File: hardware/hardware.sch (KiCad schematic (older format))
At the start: 14 parts, among them P1 CONN_13X2, Q1 Q_NPN_BCE, U1 74HC595, U2 74HC595, U3 74HC595, U4 DAC08, U5 DAC08, U6 DAC08, U7 LM555N

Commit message: Finish PWM circuitry
Note that we may have to tune the voltage going to the DAC to taste just
to make sure that Q1 isn't getting too saturated at the base.

Signed-off-by: Nkeck720 <noahkeck72@gmail.com>
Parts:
- removed Q1: Q_NPN_BCE, symbol Q_NPN_BCE
- added Q?: PN2222A, symbol PN2222A
- added U?: NCP1117ST20T3G, TO_SOT_Packages_SMD:SOT-223, symbol NCP1117ST20T3G
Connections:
- wire segments 65 -> 69
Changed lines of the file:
@@
 Wire Wire Line
 	8750 2250 8750 1950
-$Comp
-L Q_NPN_BCE Q1
-U 1 1 592B0265
-P 8850 1400
-F 0 "Q1" H 8750 1600 50  0000 R CNN
-F 1 "Q_NPN_BCE" H 8750 1500 50  0000 R CNN
-F 2 "" H 9050 1500 50  0000 C CNN
-F 3 "" H 8850 1400 50  0000 C CNN
-	1    8850 1400
-	-1   0    0    -1
-$EndComp
 Wire Wire Line
 	8750 1600 8750 1650
@@
 Text Notes 700  5650 0    60   ~ 0
 SCLK/RCLK needs to be set at 300 baud, will a 555 be stable enough or will\nwe need a crystal oscillator?
+$Comp
+L PN2222A Q?
+U 1 1 592B2515
+P 8850 1400
+F 0 "Q?" H 8700 1250 50  0000 L CNN
+F 1 "PN2222A" H 8450 1550 50  0000 L CNN
+F 2 "" H 9050 1325 50  0000 L CIN
+F 3 "" H 8850 1400 50  0000 L CNN
+	1    8850 1400
+	-1   0    0    -1
+$EndComp
+Text GLabel 3100 850  0    60   Input ~ 0
++5
+$Comp
+L NCP1117ST20T3G U?
+U 1 1 592B388B
+P 3600 850
+F 0 "U?" H 3600 1075 50  0000 C CNN
+F 1 "NCP1117ST20T3G" H 3600 1000 50  0000 C CNN
+F 2 "TO_SOT_Packages_SMD:SOT-223" H 3650 600 50  0001 L CNN
+F 3 "" H 3600 850 50  0000 C CNN
+	1    3600 850
+	1    0    0    -1
+$EndComp
+Wire Wire Line
+	3300 850  3100 850
+$Comp
+L GND #PWR?
+U 1 1 592B3959
+P 3600 1150
+F 0 "#PWR?" H 3600 900 50  0001 C CNN
+F 1 "GND" H 3600 1000 50  0000 C CNN
+F 2 "" H 3600 1150 50  0000 C CNN
+F 3 "" H 3600 1150 50  0000 C CNN
+	1    3600 1150
+	1    0    0    -1
+$EndComp
+Wire Wire Line
+	3900 850  6700 850
+Wire Wire Line
+	6700 850  6700 2200
+Wire Wire Line
+	6700 2200 6450 2200
+$Comp
+L GND #PWR?
+U 1 1 592B39F2
+P 6450 2400
+F 0 "#PWR?" H 6450 2150 50  0001 C CNN
+F 1 "GND" H 6450 2250 50  0000 C CNN
+F 2 "" H 6450 2400 50  0000 C CNN
+F 3 "" H 6450 2400 50  0000 C CNN
+	1    6450 2400
+	1    0    0    -1
+$EndComp
 $EndSCHEMATC

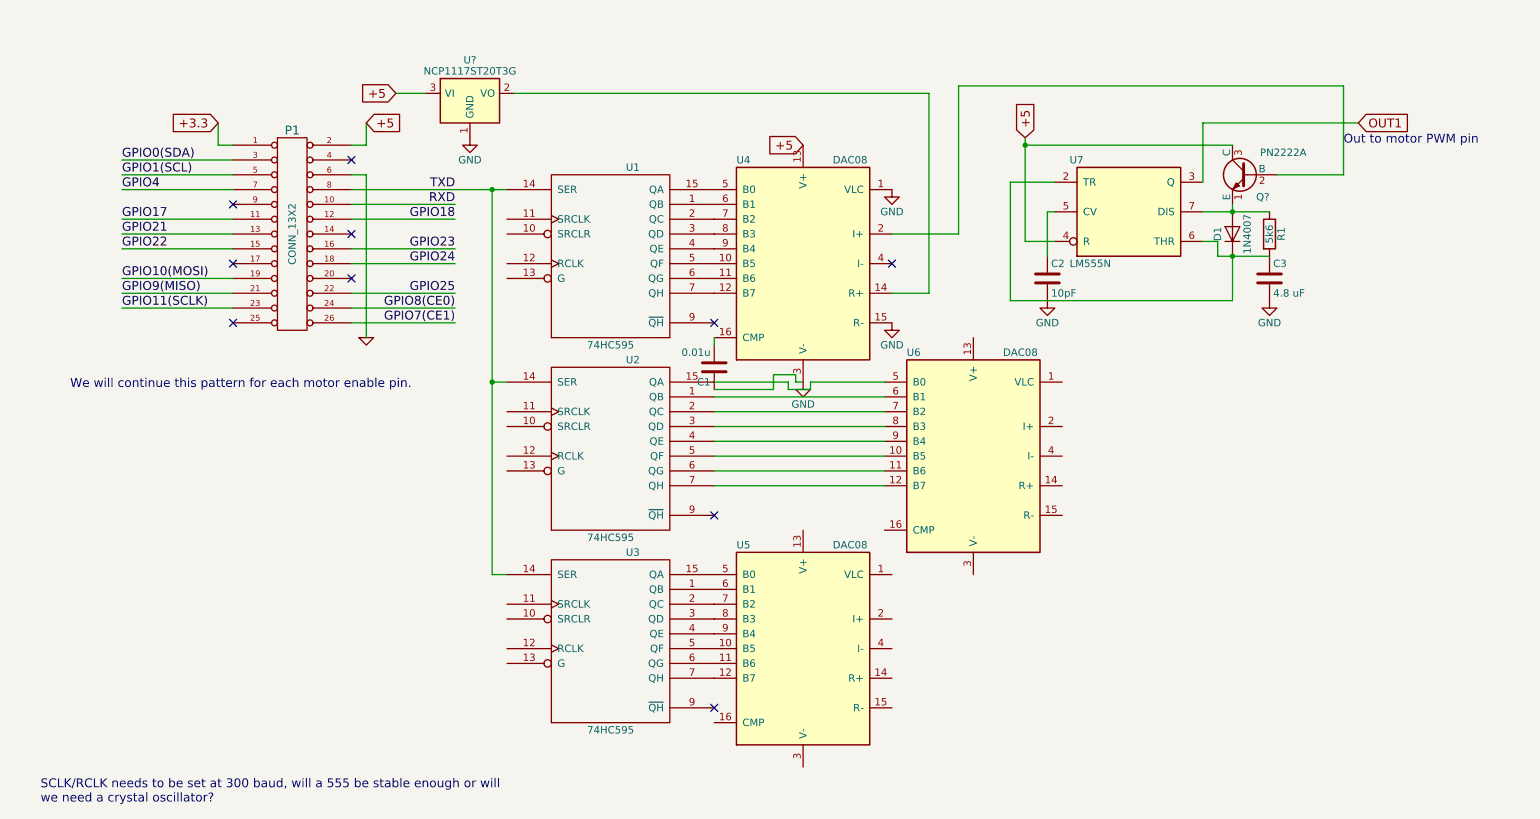
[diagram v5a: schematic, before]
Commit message: Finished perliminary support circuit
I finished the design for the support ciruitry. All I need to do now is
make a PCB layout with all of this and test with our prototype.

Signed-off-by: Nkeck720 <noahkeck72@gmail.com>
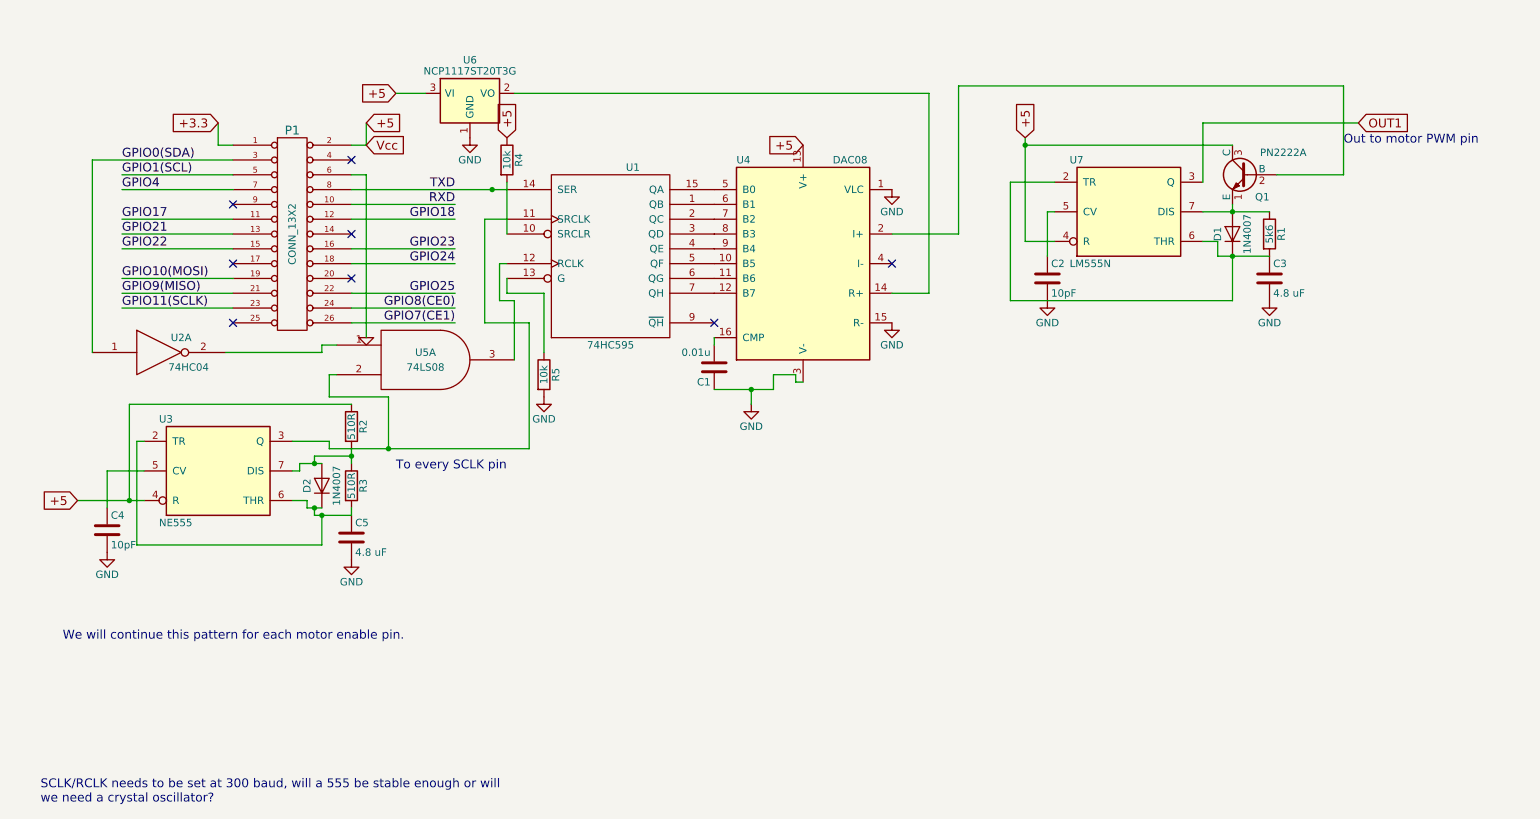
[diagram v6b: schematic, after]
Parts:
- removed U2, U3: 74HC595, symbol 74HC595
- removed U5, U6: DAC08, symbol DAC08
- added C4: 10pF, symbol C
- added C5: 4.8 uF, symbol C
- added D2: 1N4007, symbol D
- added R2, R3: 510R, symbol R
- added R4, R5: 10k, symbol R
- added U2: 74HC04, symbol 74HC04
- added U3: NE555, symbol NE555
- added U5: 74LS08, symbol 74LS08
- gave numbers to parts that had none: 2
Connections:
- net +5: now also R2.1, R4.1, U3.4 (R)
- net GND: now also C4.2, C5.2, R5.2, U2.7 (GND), U3.1 (GND), U5.7 (GND)
- net GPIO0(SDA): now also U2.1
- net VCC: now also U2.14 (VCC), U3.8 (VCC), U5.14 (VCC)
- net at U1.10 (SRCLR): now also R4.2
- net at U1.11 (SRCLK): now also U3.3 (Q), U5.2
- net at U1.12 (RCLK): now also U5.3
- net at U1.13 (G): now also R5.1
- new net: C5.1, D2.1 (K), R3.2, U3.2 (TR), U3.6 (THR)
- new net: C4.1, U3.5 (CV)
- new net: D2.2 (A), R2.2, R3.1, U3.7 (DIS)
- new net: U2.2, U5.1
- no-connect marks 10 -> 8
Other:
- note added: "To every SCLK pin"

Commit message: Fix hardware bug
I didn't need the motor enable lines to be inverted, so I removed the
inverter.

Signed-off-by: Nkeck720 <noahkeck72@gmail.com>
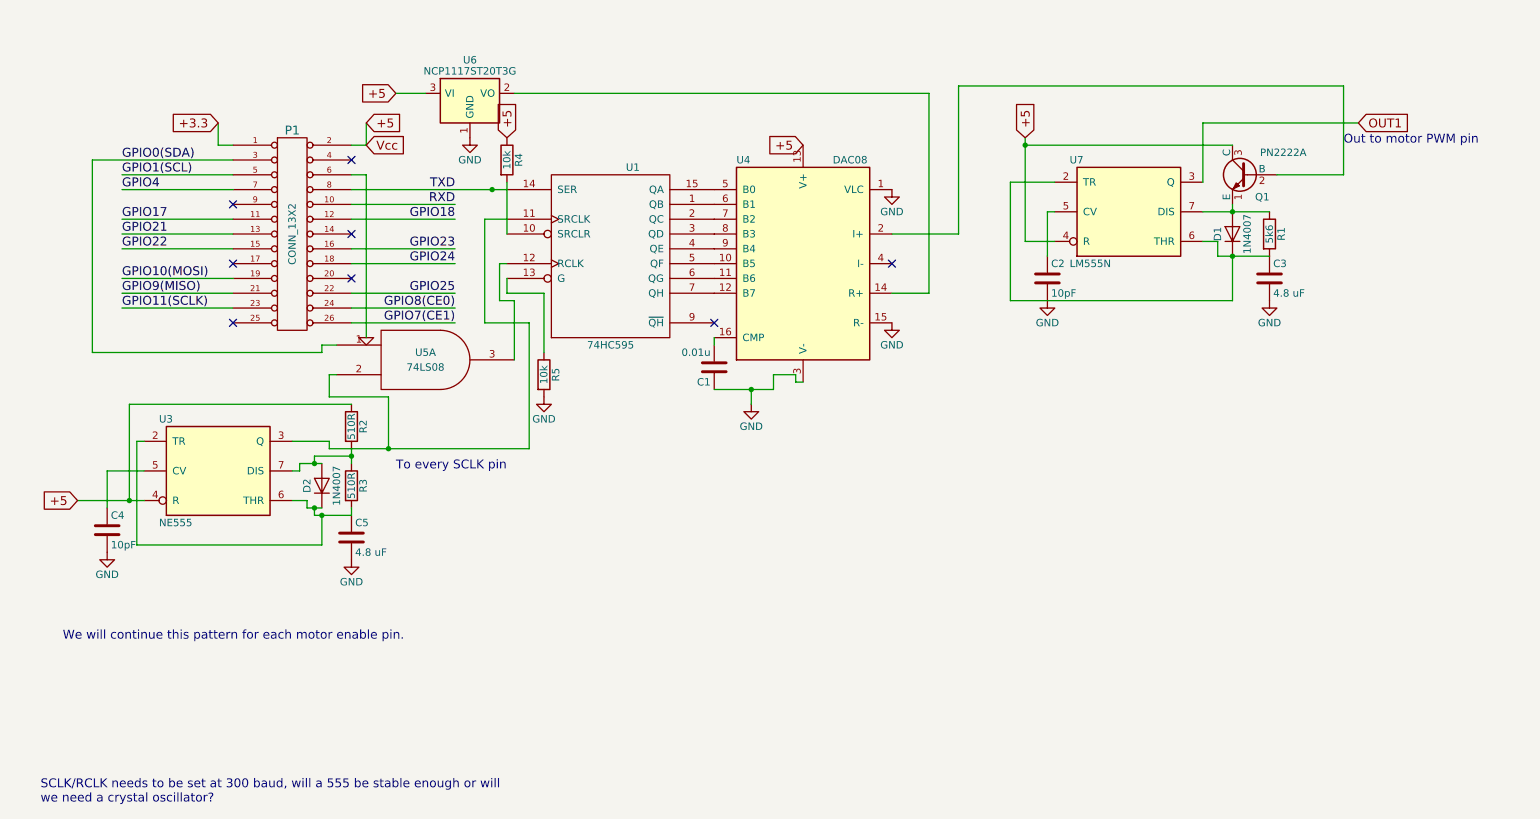
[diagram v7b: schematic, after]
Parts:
- removed U2: 74HC04, symbol 74HC04
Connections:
- net GPIO0(SDA): now also U5.1
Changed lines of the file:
@@
 	2900 1400 2800 1400
 Wire Wire Line
-	2800 1500 3850 1500
+	2800 1500 3750 1500
+Wire Wire Line
+	3750 1500 3850 1500
 Wire Wire Line
 	2800 1600 3500 1600
@@
 	5250 2550 5250 2500
 Wire Wire Line
-	5250 2850 5650 2850
+	5250 2850 5500 2850
+Wire Wire Line
+	5500 2850 5650 2850
 Wire Wire Line
 	5650 2850 5650 2750
@@
 +5
 Wire Wire Line
-	7350 1150 7350 1850
+	7350 1150 7350 1200
+Wire Wire Line
+	7350 1200 7350 1850
 Wire Wire Line
 	7350 1850 7550 1850
@@
 $EndComp
 Wire Wire Line
-	8650 1950 9000 1950
+	8650 1950 8750 1950
+Wire Wire Line
+	8750 1950 9000 1950
 Connection ~ 8750 1950
 Wire Wire Line
-	8550 1650 9000 1650
+	8550 1650 8750 1650
+Wire Wire Line
+	8750 1650 9000 1650
 Connection ~ 8750 1650
 Wire Wire Line
@@
 +5
 Wire Wire Line
-	950  3600 1400 3600
+	950  3600 1300 3600
+Wire Wire Line
+	1300 3600 1400 3600
 $Comp
 L D D2
@@
 $EndComp
 Wire Wire Line
-	2450 3350 2600 3350
+	2450 3350 2550 3350
+Wire Wire Line
+	2550 3350 2600 3350
 Wire Wire Line
 	2450 3350 2450 3400
@@
 	2500 3600 2500 3650
 Wire Wire Line
-	2500 3650 2600 3650
+	2500 3650 2550 3650
+Wire Wire Line
+	2550 3650 2600 3650
 Wire Wire Line
 	2550 3350 2550 3300
@@
 	2550 3650 2550 3700
 Wire Wire Line
-	2550 3700 2800 3700
+	2550 3700 2600 3700
+Wire Wire Line
+	2600 3700 2800 3700
 Connection ~ 2550 3650
 $Comp
@@
 $EndComp
 Wire Wire Line
-	2800 3250 2800 3350
+	2800 3250 2800 3300
+Wire Wire Line
+	2800 3300 2800 3350
 Connection ~ 2800 3300
 Wire Wire Line
@@
 	1350 3200 1400 3200
 Connection ~ 2600 3700
-$Comp
-L 74HC04 U2
-U 1 1 592B80C8
-P 1500 2600
-F 0 "U2" H 1650 2700 50  0000 C CNN
-F 1 "74HC04" H 1700 2500 50  0000 C CNN
-F 2 "" H 1500 2600 50  0000 C CNN
-F 3 "" H 1500 2600 50  0000 C CNN
-	1    1500 2600
-	1    0    0    -1
-$EndComp
 Wire Wire Line
 	1050 2600 1050 1300
@@
 	2650 3200 2650 3250
 Wire Wire Line
-	2650 3250 4000 3250
+	2650 3250 3050 3250
+Wire Wire Line
+	3050 3250 4000 3250
 Wire Wire Line
 	4000 3250 4000 2400
@@
 $EndComp
 Wire Wire Line
-	1950 2600 2600 2600
+	1050 2600 2600 2600
 Wire Wire Line
 	2600 2600 2600 2550
@@
 Text GLabel 3850 1150 1    60   Input ~ 0
 +5
-Wire Wire Line
-	3850 1800 3850 1450
 $Comp
 L R R5
@@
 	1    0    0    -1
 $EndComp
+Wire Wire Line
+	3850 1800 3850 1450
 $EndSCHEMATC

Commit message: Start Final PCB design/layout
Signed-off-by: Nkeck720 <noahkeck72@gmail.com>
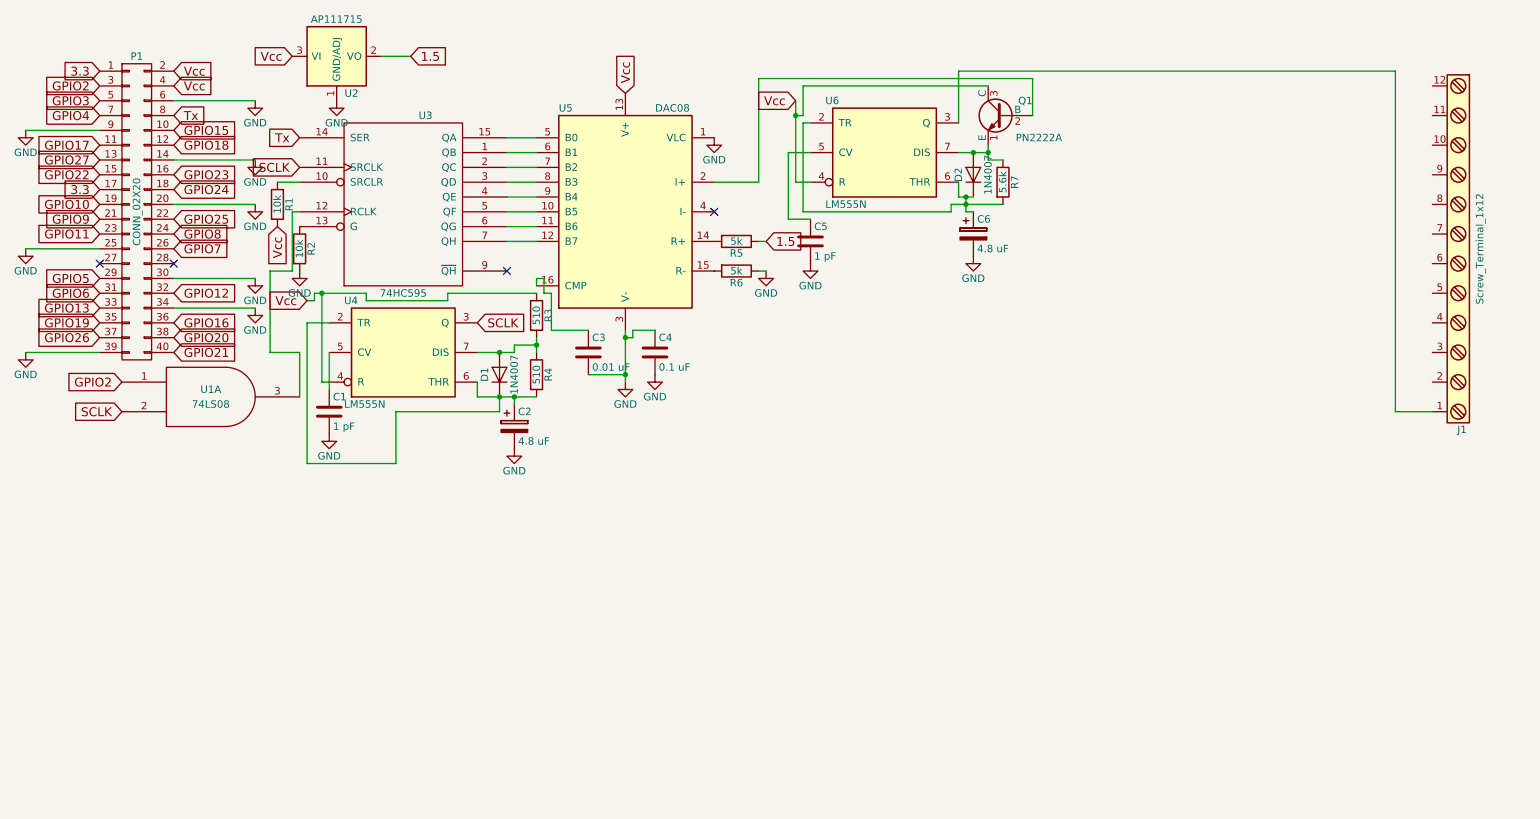
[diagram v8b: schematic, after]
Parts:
- removed C2: 10pF, symbol C
- removed P1: CONN_13X2, symbol CONN_13X2
- removed U1: 74HC595, symbol 74HC595
- removed U3: NE555, symbol NE555
- removed U4: DAC08, symbol DAC08
- removed U5: 74LS08, symbol 74LS08
- removed U6: NCP1117ST20T3G, TO_SOT_Packages_SMD:SOT-223, symbol NCP1117ST20T3G
- removed U7: LM555N, symbol LM555N
- added C2, C6: 4.8 uF, symbol CP
- added J1: Screw_Terminal_1x12, symbol Screw_Terminal_1x12
- added P1: CONN_02X20, symbol CONN_02X20
- added R6: 5k, symbol R
- added R7: 5.6k, symbol R
- added U1: 74LS08, symbol 74LS08
- added U2: AP111715, TO_SOT_Packages_SMD:SOT-223, symbol AP111715
- added U3: 74HC595, symbol 74HC595
- added U4, U6: LM555N, symbol LM555N
- added U5: DAC08, symbol DAC08
- C1: value 0.01u -> 1 pF
- C3: value 4.8 uF -> 0.01 uF
- C4: value 10pF -> 0.1 uF
- C5: value 4.8 uF -> 1 pF
- R1: value 5k6 -> 10k
- R2: value 510R -> 10k
- R3: value 510R -> 510
- R4: value 10k -> 510
- R5: value 10k -> 5k
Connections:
- net GND: now also C1.2, C4.1, R2.2, C2.2, C6.2, P1.14 (P14), P1.20 (P20), P1.25 (P25), P1.30 (P30), P1.34 (P34), P1.39 (P39), P1.6 (P6), P1.9 (P9), R6.1, U1.7 (GND), U2.1 (GND/ADJ), U3.8 (GND), U4.1 (GND), U5.1 (VLC), U5.3 (V-), U6.1 (GND); no longer C1.1, R5.2
- net GPIO17: now also P1.11 (P11)
- net GPIO18: now also P1.12 (P12)
- net GPIO21: now also P1.40 (P40)
- net GPIO22: now also P1.15 (P15)
- net GPIO23: now also P1.16 (P16)
- net GPIO24: now also P1.18 (P18)
- net GPIO25: now also P1.22 (P22)
- net GPIO4: now also P1.7 (P7)
- net VCC: now also U1.14 (VCC), U3.16 (VCC), U4.8 (VCC), U6.8 (VCC)
- net at R4.2: now also D1.1 (K), C2.1, U4.2 (TR), U4.6 (THR)
- net 1.5: now reaches R5.1
- net 1.5: now also U2.2 (VO), U2.4 (VO)
- net at Q1.2 (B): now also U5.2 (I+)
- removed net +5: Q1.3 (C), R2.1, R4.1
- new net: U3.1 (QB), U5.6 (B1)
- new net: R1.1, U3.10 (SRCLR)
- new net: U1.3, U3.12 (RCLK)
- new net: R2.1, U3.13 (G)
- new net: U3.15 (QA), U5.5 (B0)
- new net: U3.2 (QC), U5.7 (B2)
- new net: U3.3 (QD), U5.8 (B3)
- new net: U3.4 (QE), U5.9 (B4)
- new net: U3.5 (QF), U5.10 (B5)
- new net: U3.6 (QG), U5.11 (B6)
- new net: U3.7 (QH), U5.12 (B7)
- new net: C1.1, U4.5 (CV)
- new net: D1.2 (A), R3.2, R4.1, U4.7 (DIS)
- new net: R5.2, U5.14 (R+)
- new net: R6.2, U5.15 (R-)
- new net: C3.1, U5.16 (CMP)
- new net: C6.1, D2.1 (K), R7.2, U6.2 (TR), U6.6 (THR)
- new net: J1.1, U6.3 (Q)
- new net: C5.1, U6.5 (CV)
- new net: D2.2 (A), Q1.1 (E), R7.1, U6.7 (DIS)
- new net 3.3: P1.1 (P1), P1.17 (P17)
- new net GPIO10: P1.19 (P19)
- new net GPIO11: P1.23 (P23)
- new net GPIO12: P1.32 (P32)
- new net GPIO13: P1.33 (P33)
- new net GPIO15: P1.10 (P10)
- new net GPIO16: P1.36 (P36)
- new net GPIO19: P1.35 (P35)
- new net GPIO2: P1.3 (P3), U1.1
- new net GPIO20: P1.38 (P38)
- new net GPIO26: P1.37 (P37)
- new net GPIO27: P1.13 (P13)
- new net GPIO3: P1.5 (P5)
- new net GPIO5: P1.29 (P29)
- new net GPIO6: P1.31 (P31)
- new net GPIO7: P1.26 (P26)
- new net GPIO8: P1.24 (P24)
- new net GPIO9: P1.21 (P21)
- new net SCLK: U1.2, U3.11 (SRCLK), U4.3 (Q)
- new net Tx: P1.8 (P8), U3.14 (SER)
- new net Vcc: P1.2 (P2), P1.4 (P4), Q1.3 (C), R1.2, R3.1, U2.3 (VI), U4.4 (R), U5.13 (V+), U6.4 (R)
- no-connect marks 8 -> 4
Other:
- note removed: "Out to motor PWM pin"
- note removed: "SCLK/RCLK needs to be set at 300 baud, will a 555 be stable enough or will\nwe need a crystal oscillator?"
- note removed: "To every SCLK pin"
- note removed: "We will continue this pattern for each motor enable pin."
